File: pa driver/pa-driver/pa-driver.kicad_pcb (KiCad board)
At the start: 2 copper layers, 54.6 x 34.3 mm, 18 parts, among them J1 Power Connector, Q1 PN2222A, T1 Transformer_1P_2S

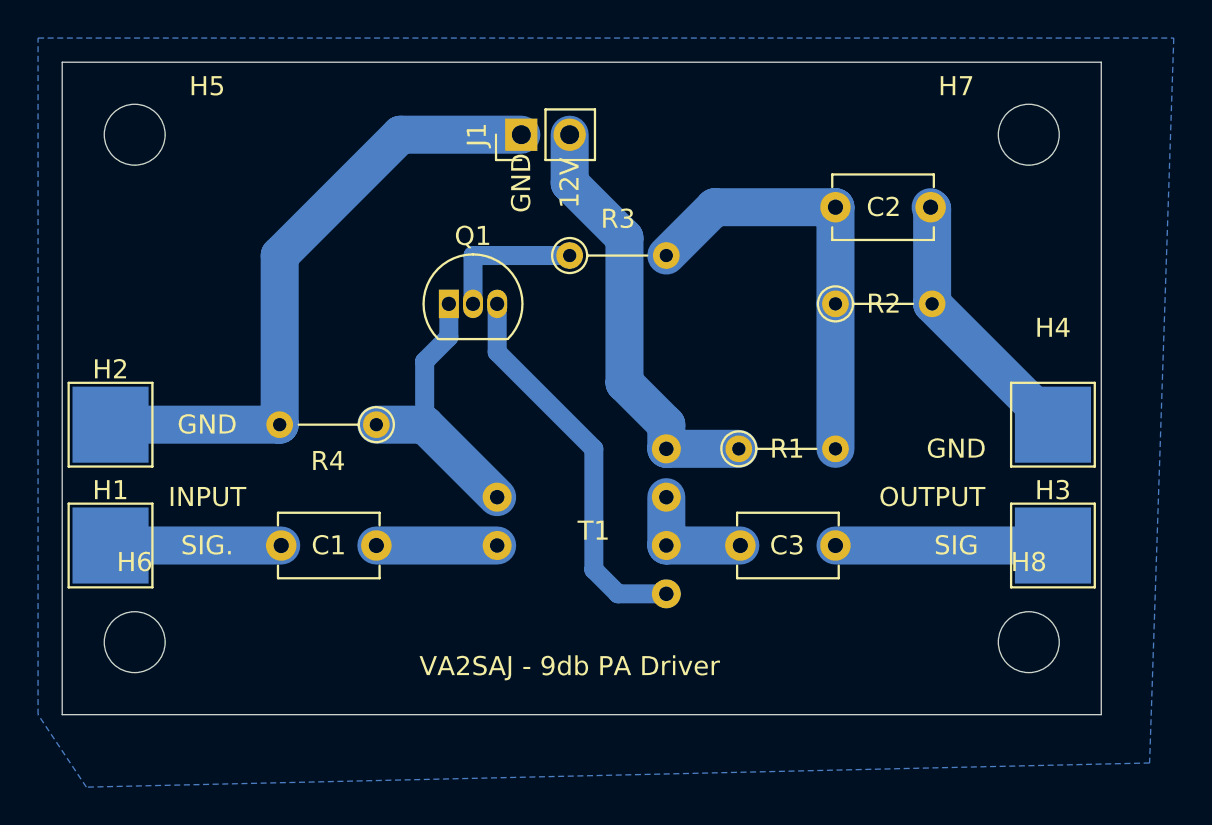
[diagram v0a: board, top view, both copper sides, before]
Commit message: Modif to PA driver
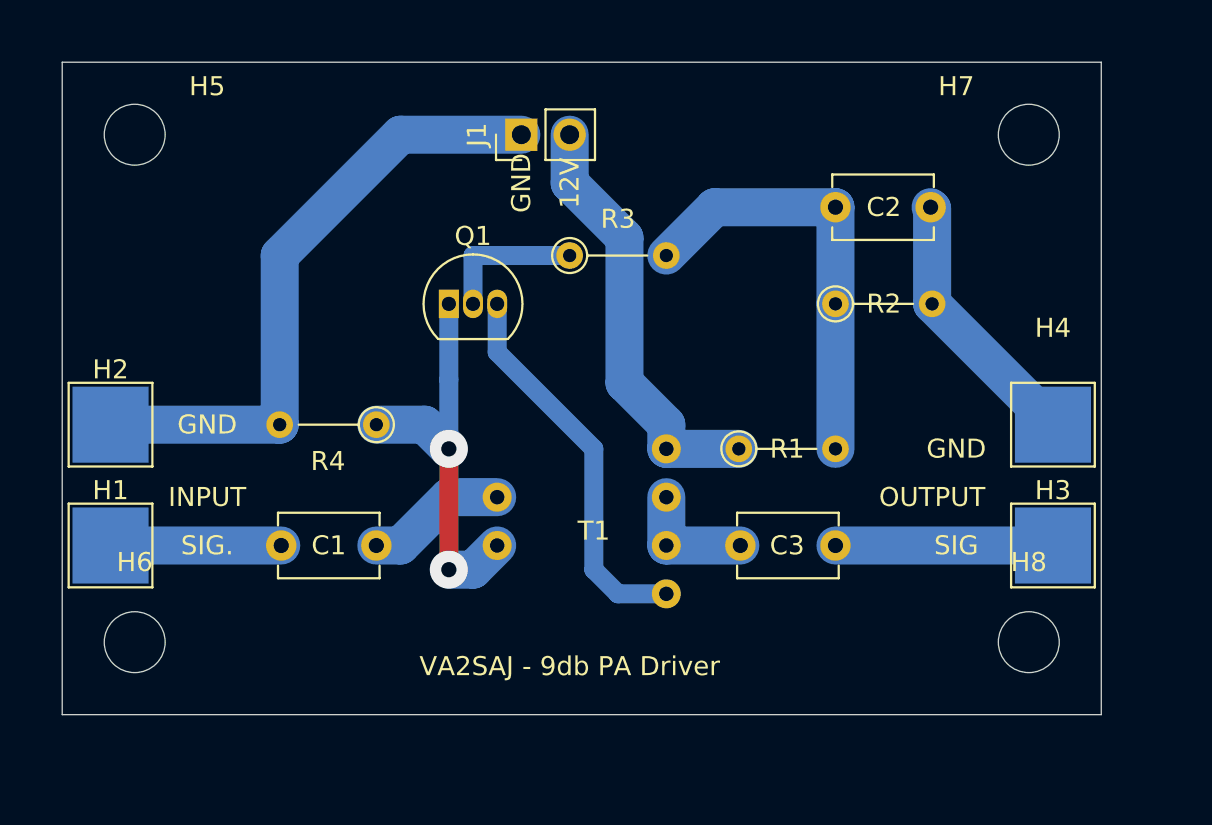
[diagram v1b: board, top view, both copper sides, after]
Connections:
- T1 pad 1: Net-(Q1-Pad1) -> Net-(C1-Pad1)
- T1 pad 2: Net-(C1-Pad1) -> Net-(Q1-Pad1)
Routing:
- net Net-(Q1-Pad1): track 14.8 -> 21.4 mm, vias 0 -> 2
- net Net-(C1-Pad1): track 6.35 -> 7.40 mm
- removed copper zone on B.Cu, net GND
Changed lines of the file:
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@@
     (thickness 1.6)
     (drawings 13)
-    (tracks 34)
+    (tracks 42)
     (zones 0)
     (modules 18)
@@
   )
   (setup
-    (last_trace_width 0.25)
+    (last_trace_width 2)
     (user_trace_width 1)
     (user_trace_width 2)
@@
       (net 10 +12V))
     (pad 2 thru_hole circle (at -5.08 1.27) (size 1.524 1.524) (drill 0.762) (layers *.Cu *.Mask)
+      (net 1 "Net-(Q1-Pad1)"))
+    (pad 1 thru_hole circle (at -5.08 -1.27) (size 1.524 1.524) (drill 0.762) (layers *.Cu *.Mask)
       (net 5 "Net-(C1-Pad1)"))
-    (pad 1 thru_hole circle (at -5.08 -1.27) (size 1.524 1.524) (drill 0.762) (layers *.Cu *.Mask)
-      (net 1 "Net-(Q1-Pad1)"))
   )
   (module TestPoint:TestPoint_Pad_4.0x4.0mm (layer F.Cu)
@@
       (effects (font (size 1 1) (thickness 0.15)))
     )
-    (fp_text value 100nf (at 6.35 -2.54) (layer F.Fab)
+    (fp_text value 100nf (at 2.54 -2.54) (layer F.Fab)
       (effects (font (size 1 1) (thickness 0.15)))
     )
@@
   (gr_line (start 72.39 93.98) (end 127 93.98) (layer Edge.Cuts) (width 0.05))
   (gr_line (start 72.39 128.27) (end 72.39 93.98) (layer Edge.Cuts) (width 0.05))
-  (segment (start 91.44 113.03) (end 95.25 116.84) (width 2) (layer B.Cu) (net 1))
+  (segment (start 92.71 106.68) (end 92.71 110.659999) (width 1) (layer B.Cu) (net 1))
+  (segment (start 92.71 110.659999) (end 92.71 114.3) (width 1) (layer B.Cu) (net 1))
+  (segment (start 92.71 114.3) (end 92.71 114.3) (width 1) (layer B.Cu) (net 1))
+  (via (at 92.71 114.3) (size 2) (drill 0.8) (layers F.Cu B.Cu) (net 1))
+  (segment (start 92.71 120.65) (end 92.71 120.65) (width 1) (layer B.Cu) (net 1))
+  (via (at 92.71 120.65) (size 2) (drill 0.8) (layers F.Cu B.Cu) (net 1))
+  (segment (start 92.71 114.3) (end 92.71 120.65) (width 1) (layer F.Cu) (net 1))
+  (segment (start 91.44 113.03) (end 92.71 114.3) (width 2) (layer B.Cu) (net 1))
   (segment (start 88.9 113.03) (end 91.44 113.03) (width 2) (layer B.Cu) (net 1))
-  (segment (start 91.44 109.7) (end 91.44 113.03) (width 1) (layer B.Cu) (net 1))
-  (segment (start 92.71 108.43) (end 91.44 109.7) (width 1) (layer B.Cu) (net 1))
-  (segment (start 92.71 106.68) (end 92.71 108.43) (width 1) (layer B.Cu) (net 1))
+  (segment (start 93.98 120.65) (end 95.25 119.38) (width 2) (layer B.Cu) (net 1))
+  (segment (start 92.71 120.65) (end 93.98 120.65) (width 2) (layer B.Cu) (net 1))
   (segment (start 101.6 121.92) (end 104.14 121.92) (width 1) (layer B.Cu) (net 2))
   (segment (start 100.33 120.65) (end 101.6 121.92) (width 1) (layer B.Cu) (net 2))
@@
   (segment (start 93.98 104.14) (end 99.06 104.14) (width 1) (layer B.Cu) (net 3))
   (segment (start 74.93 119.38) (end 83.9 119.38) (width 2) (layer B.Cu) (net 4))
-  (segment (start 88.9 119.38) (end 95.25 119.38) (width 2) (layer B.Cu) (net 5))
-  (segment (start 74.93 113.03) (end 83.82 113.03) (width 2) (layer B.Cu) (net 6))
+  (segment (start 88.9 119.38) (end 90.17 119.38) (width 2) (layer B.Cu) (net 5))
+  (segment (start 92.71 116.84) (end 95.25 116.84) (width 2) (layer B.Cu) (net 5))
+  (segment (start 90.17 119.38) (end 92.71 116.84) (width 2) (layer B.Cu) (net 5))
   (segment (start 118.11 106.68) (end 124.46 113.03) (width 2) (layer B.Cu) (net 6))
   (segment (start 118.11 101.68) (end 118.03 101.6) (width 2) (layer B.Cu) (net 6))
   (segment (start 118.11 106.68) (end 118.11 101.68) (width 2) (layer B.Cu) (net 6))
-  (segment (start 83.82 113.03) (end 83.82 104.14) (width 2) (layer B.Cu) (net 6))
+  (segment (start 74.93 113.03) (end 83.82 113.03) (width 2) (layer B.Cu) (net 6))
   (segment (start 90.17 97.79) (end 96.52 97.79) (width 2) (layer B.Cu) (net 6))
   (segment (start 83.82 104.14) (end 90.17 97.79) (width 2) (layer B.Cu) (net 6))
+  (segment (start 83.82 113.03) (end 83.82 104.14) (width 2) (layer B.Cu) (net 6))
   (segment (start 113.03 114.3) (end 113.03 106.68) (width 2) (layer B.Cu) (net 7))
   (segment (start 113.03 106.68) (end 113.03 101.6) (width 2) (layer B.Cu) (net 7))
@@
   (segment (start 104.14 113.03) (end 104.14 114.3) (width 2) (layer B.Cu) (net 10))
   (segment (start 101.939992 110.829992) (end 104.14 113.03) (width 2) (layer B.Cu) (net 10))
-  (zone (net 6) (net_name GND) (layer B.Cu) (hatch edge 0.508)
-    (connect_pads (clearance 0.508))
-    (min_thickness 0.254)
-    (fill yes (arc_segments 32) (thermal_gap 0.508) (thermal_bridge_width 0.508))
-    (polygon
-      (pts
-        (xy 129.54 130.81) (xy 73.66 132.08) (xy 71.12 128.27) (xy 71.12 92.71) (xy 130.81 92.71)
-      )
-    )
-  )
 )
